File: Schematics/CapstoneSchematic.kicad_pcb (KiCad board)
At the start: 2 copper layers, 151.1 x 60.8 mm, 15 parts, among them J1 ArduinoRGBShield, J2 VoltageIn, T1 Temp Sensor, U6 LaserSensor

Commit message: finished pcb
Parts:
- SAS1: footprint TerminalBlock_MetzConnect:TerminalBlock_MetzConnect_Type094_RT03503HBLU_1x03_P5.00mm_Horizontal -> TerminalBlock_MetzConnect:TerminalBlock_MetzConnect_Type094_RT03502HBLU_1x02_P5.00mm_Horizontal
- SAS2: footprint TerminalBlock_MetzConnect:TerminalBlock_MetzConnect_Type094_RT03502HBLU_1x02_P5.00mm_Horizontal -> TerminalBlock_MetzConnect:TerminalBlock_MetzConnect_Type094_RT03503HBLU_1x03_P5.00mm_Horizontal
- moved LR1 57.0 mm to (113.5, 124.5), turned to 90 degrees
- moved SAS2 22.0 mm to (118.2, 123.5), turned to 0 degrees
- moved MPS2 10.9 mm to (146.8, 123.5), turned to 0 degrees
- moved SAS1 6.93 mm to (135.0, 123.5), turned to 0 degrees
- moved MPS1 0.44 mm to (98.5, 114.5)
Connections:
- A1 pad 15: Net-(A1-Pad15) -> /LoRa4
- A1 pad 16: Net-(A1-Pad16) -> /LoRa3
- A1 pad 17: Net-(A1-Pad17) -> /SAS_Int1
- A1 pad 18: Net-(A1-Pad18) -> /SAS_Int2
- A1 pad 20: Net-(A1-Pad20) -> /LoRa2
- A1 pad 21: Net-(A1-Pad21) -> /LED_R
- A1 pad 22: Net-(A1-Pad22) -> /LED_G
- A1 pad 24: Net-(A1-Pad24) -> /IN1
- A1 pad 25: Net-(A1-Pad25) -> /IN2
- J2 pad 1: 0 -> +12V
- J2 pad 2: +12V -> 0
- LED_GREEN1 pad 2: Net-(A1-Pad23) -> /LED_G
- LED_RED1 pad 2: Net-(A1-Pad24) -> /LED_R
- MPS1 pad 3: Net-(A1-Pad20) -> Net-(A1-Pad27)
- MPS2 pad 3: Net-(A1-Pad21) -> Net-(A1-Pad28)
- PR1 pad 2: Net-(A1-Pad9) -> Net-(A1-Pad11)
- RM1 pad 2: Net-(A1-Pad27) -> /IN1
- RM1 pad 3: Net-(A1-Pad28) -> /IN2
- SAS2 pad 2: Net-(SAS2-Pad2) -> Net-(RM1-Pad6)
- U6 pad 3: Net-(A1-Pad26) -> Net-(A1-Pad19)
- ULoRa1 pad 2: Net-(A1-Pad19) -> /LoRa2
- ULoRa1 pad 3: Net-(A1-Pad15) -> /LoRa3
- ULoRa1 pad 4: Net-(A1-Pad16) -> /LoRa4
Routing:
- net /SAS_Int2: track 0.00 -> 112.6 mm, vias 0 -> 1
- net Net-(A1-Pad27): track 0.00 -> 110.1 mm, vias 0 -> 1
- net /SAS_Int1: track 0.00 -> 103.4 mm, vias 0 -> 1
- net Net-(A1-Pad28): track 0.00 -> 69.4 mm, vias 0 -> 1
- net +12V: track 9.34 -> 78.4 mm, vias 0 -> 1
- net Net-(A1-Pad13): track 0.00 -> 52.8 mm
- net /IN1: track 0.00 -> 50.4 mm, vias 0 -> 1
- net Net-(RM1-Pad6): track 0.00 -> 43.9 mm, vias 0 -> 1
- net /IN2: track 0.00 -> 43.9 mm, vias 0 -> 1
- net 0: track 8.71 -> 49.3 mm
- net /LoRa2: track 0.00 -> 27.7 mm
- net /LoRa4: track 0.00 -> 27.3 mm
- net /LoRa3: track 0.00 -> 24.6 mm
- net /LED_G: track 0.00 -> 22.4 mm
- net Net-(A1-Pad24): track 17.9 -> 0.00 mm
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- added copper zone on F.Cu, net +5V
- added copper zone on B.Cu, net GND
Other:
- board text added: "Im hesitant about layering these two"

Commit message: Fixed a layer
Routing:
- net Net-(A1-Pad14): track 49.2 -> 52.8 mm
- net +5V: track 0.00 -> 2.50 mm, vias 0 -> 2
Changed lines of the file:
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@@
     (thickness 1.6)
     (drawings 9)
-    (tracks 108)
+    (tracks 113)
     (zones 0)
     (modules 15)
@@
   (segment (start 229.884999 124.200001) (end 229.085 125) (width 0.25) (layer B.Cu) (net 1))
   (segment (start 234.224999 119.860001) (end 229.884999 124.200001) (width 0.25) (layer B.Cu) (net 1))
-  (segment (start 234.224999 79.570001) (end 234.224999 119.860001) (width 0.25) (layer B.Cu) (net 1))
-  (segment (start 235.4 78.395) (end 234.224999 79.570001) (width 0.25) (layer B.Cu) (net 1))
-  (segment (start 232 90) (end 232 90) (width 0.25) (layer B.Cu) (net 2))
+  (segment (start 234.197919 78.395) (end 230.77 81.822919) (width 0.25) (layer B.Cu) (net 1))
+  (segment (start 235.4 78.395) (end 234.197919 78.395) (width 0.25) (layer B.Cu) (net 1))
+  (segment (start 230.77 81.822919) (end 230.77 89.4) (width 0.25) (layer B.Cu) (net 1))
+  (segment (start 234.224999 92.854999) (end 234.224999 119.860001) (width 0.25) (layer B.Cu) (net 1))
+  (segment (start 230.77 89.4) (end 234.224999 92.854999) (width 0.25) (layer B.Cu) (net 1))
   (segment (start 227.344999 124.200001) (end 226.545 125) (width 0.25) (layer F.Cu) (net 2))
   (segment (start 234.224999 117.320001) (end 227.344999 124.200001) (width 0.25) (layer F.Cu) (net 2))
@@
   (segment (start 219.9 120.895) (end 224.005 125) (width 0.25) (layer F.Cu) (net 3))
   (segment (start 219.9 117.675) (end 219.9 120.895) (width 0.25) (layer F.Cu) (net 3))
+  (via (at 217.5 82) (size 0.8) (drill 0.4) (layers F.Cu B.Cu) (net 6))
+  (via (at 220 82) (size 0.8) (drill 0.4) (layers F.Cu B.Cu) (net 6))
+  (segment (start 217.5 82) (end 220 82) (width 0.25) (layer B.Cu) (net 6))
   (segment (start 203.05 123.095) (end 201.145 125) (width 0.25) (layer F.Cu) (net 7))
   (segment (start 203.05 117.675) (end 203.05 123.095) (width 0.25) (layer F.Cu) (net 7))
@@
   (segment (start 218.465 122) (end 221.465 125) (width 0.25) (layer F.Cu) (net 19))
   (segment (start 212.375 122) (end 218.465 122) (width 0.25) (layer F.Cu) (net 19))
-  (segment (start 204.705 85.27) (end 204.5 85.475) (width 0.25) (layer F.Cu) (net 37))
   (segment (start 230 97.08) (end 232 99.08) (width 0.25) (layer B.Cu) (net 29))
   (segment (start 226.545 76.74) (end 230 80.195) (width 0.25) (layer B.Cu) (net 29))
@@
   (segment (start 205.045 83) (end 211.305 76.74) (width 0.25) (layer F.Cu) (net 36))
   (segment (start 195.02 83) (end 205.045 83) (width 0.25) (layer F.Cu) (net 36))
+  (segment (start 204.705 85.27) (end 204.5 85.475) (width 0.25) (layer F.Cu) (net 37))
   (segment (start 204.5 85.475) (end 206.475 83.5) (width 0.25) (layer F.Cu) (net 37))
   (segment (start 207.085 83.5) (end 213.845 76.74) (width 0.25) (layer F.Cu) (net 37))
@@
     (polygon
       (pts
-        (xy 87 70.5) (xy 87 130.5) (xy 237 130.5) (xy 237 70.5)
+        (xy 237 70.5) (xy 86.5 70.5) (xy 86.5 130.5) (xy 237 130.5)
       )
     )
@@
     (polygon
       (pts
-        (xy 87 70.5) (xy 87 130.5) (xy 237 130.5) (xy 237 70.5)
+        (xy 237 70.5) (xy 86.5 70.5) (xy 86.5 130.5) (xy 237 130.5)
       )
     )

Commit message: Emergency fix
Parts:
- moved MPS1 27.3 mm to (99.5, 87.2)
- moved SAS2 10.5 mm to (128.7, 123.2), turned to 180 degrees
- moved MPS2 9.95 mm to (156.7, 123.2), turned to 180 degrees
- moved SAS1 5.43 mm to (140.4, 123.2), turned to 180 degrees
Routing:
- net +12V: track 78.4 -> 45.2 mm, vias 1 -> 0
- net +3V3: track 8.11 -> 38.4 mm
- net Net-(A1-Pad8): track 119.8 -> 137.8 mm
- net /IN2: track 43.9 -> 55.9 mm, vias 1 -> 0
- net Net-(A1-Pad28): track 69.4 -> 81.3 mm
- net /IN1: track 50.4 -> 60.2 mm, vias 1 -> 0
- net /SAS_Int2: track 112.6 -> 122.0 mm, vias 1 -> 0
- net Net-(A1-Pad27): track 110.1 -> 102.3 mm, vias 1 -> 0
- net Net-(A1-Pad13): track 52.8 -> 57.8 mm, vias 0 -> 1
- net /SAS_Int1: track 103.4 -> 107.8 mm, vias 1 -> 0
- net Net-(RM1-Pad6): track 43.9 -> 40.8 mm, vias 1 -> 0
- net 0: track 49.3 -> 47.1 mm
- net +5V: track 2.50 -> 4.05 mm
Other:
- board text added: "+12V"
- board text added: "+3.3"
- board text added: "0V"
- board text added: "12V"
- board text added: "Chicken Coop PCB v1"
- board text added: "Jacob Berdichevsky Nathan Schimpf Michael Portaro Adedotun Abe"
- board text added: "Super important via"
- board text removed: "Im hesitant about layering these two"

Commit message: Fixed most of schematic, need to update linear regulator footprint
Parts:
- renumbered J2 to J1, J1 to J2, U6 to U1
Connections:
- A1 pad 1: Net-(A1-Pad1) -> (no net)
- A1 pad 10: Net-(A1-Pad10) -> (no net)
- A1 pad 15: /LoRa4 -> (no net)
- A1 pad 2: Net-(A1-Pad2) -> (no net)
- A1 pad 21: /LED_R -> (no net)
- A1 pad 22: /LED_G -> /LED_R
- A1 pad 23: Net-(A1-Pad23) -> (no net)
- A1 pad 26: Net-(A1-Pad26) -> (no net)
- A1 pad 29: Net-(A1-Pad29) -> (no net)
- A1 pad 3: Net-(A1-Pad3) -> (no net)
- A1 pad 30: Net-(A1-Pad30) -> +3V3
- A1 pad 31: Net-(A1-Pad31) -> (no net)
- A1 pad 32: Net-(A1-Pad32) -> (no net)
- A1 pad 6: Net-(A1-Pad6) -> (no net)
- A1 pad 9: Net-(A1-Pad9) -> (no net)
- LED_GREEN1 pad 2: /LED_G -> +5V
- MPS2 pad 2: GND -> Net-(RM1-Pad6)
- RM1 pad 9: +12V -> Net-(LA1-Pad2)
- SAS1 pad 1: +5V -> GND
- SAS2 pad 1: +5V -> GND
- SAS2 pad 2: Net-(RM1-Pad6) -> /SAS_Int2
- SAS2 pad 4: /SAS_Int2 -> Net-(LA1-Pad2)
- ULoRa1 pad 3: /LoRa3 -> (no net)
- ULoRa1 pad 4: /LoRa4 -> (no net)
- ULoRa1 pad 5: Net-(ULoRa1-Pad5) -> (no net)
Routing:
- net +3V3: track 38.4 -> 96.9 mm
- net (no net): track 0.00 -> 51.9 mm
- net /LoRa4: track 27.3 -> 0.00 mm
- net Net-(LA1-Pad2): track 0.00 -> 26.7 mm
- net /SAS_Int2: track 122.0 -> 147.0 mm, vias 0 -> 1
- net /LoRa3: track 24.6 -> 0.00 mm
- net /LED_G: track 22.4 -> 0.00 mm
- net Net-(RM1-Pad6): track 40.8 -> 60.0 mm
- net +5V: track 4.05 -> 1.55 mm, vias 2 -> 0

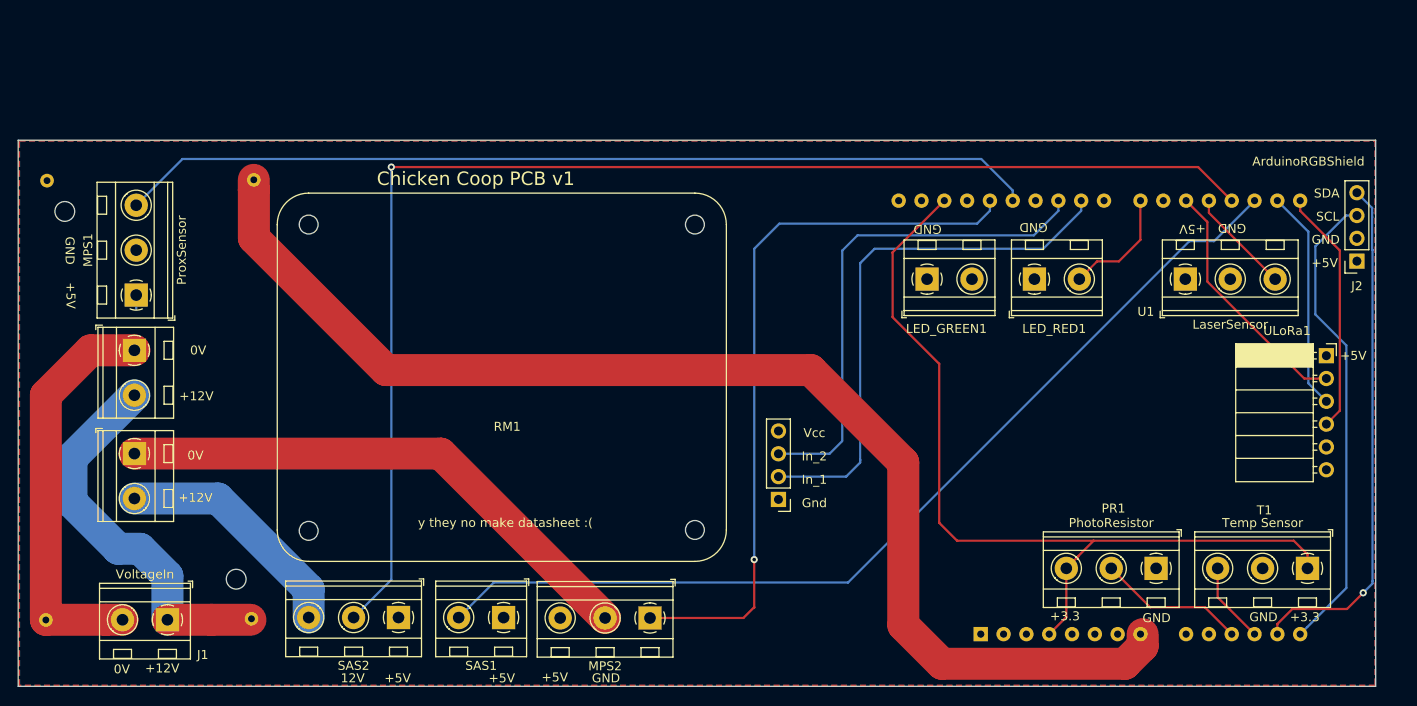
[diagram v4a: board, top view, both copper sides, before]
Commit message: Fixed Linear regulator footprint
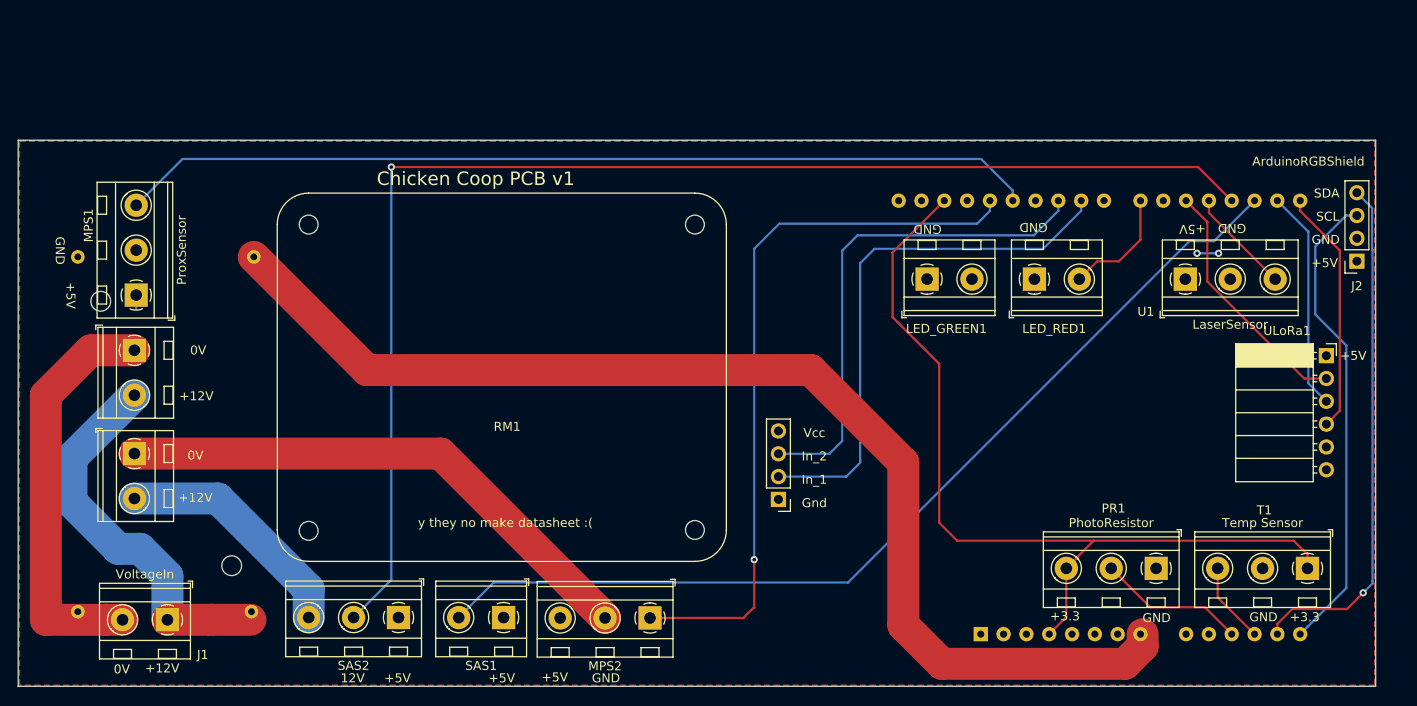
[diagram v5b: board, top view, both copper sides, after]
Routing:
- net Net-(A1-Pad8): track 137.8 -> 130.5 mm
- net +5V: track 1.55 -> 3.95 mm, vias 0 -> 2
